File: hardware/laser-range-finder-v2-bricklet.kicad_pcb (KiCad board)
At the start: 2 copper layers, 48.2 x 35.6 mm, 23 parts, among them P1 CON-SENSOR2, P2 DEBUG, P3 BOOT, P4 CONN_6, U1 XMC1XXX24, U2 DRILL, U3 DRILL, U4 DRILL, U5 DRILL

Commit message: changed pcb design
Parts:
- added G***: Logo_31x31, kicad-libraries:Logo_31x31, F.Cu at (123.9, 100.1)
- added G***: LOGO, kicad-libraries:Logo_CoMCU, F.Cu at (146.2, 97.2)
- added VAL: CE_5mm, kicad-libraries:CE_5mm, F.Cu at (146.3, 103.4)
- added VAL: WEEE_7mm, kicad-libraries:WEEE_7mm, F.Cu at (145.2, 109.2)
- moved D1 31.0 mm to (156.8, 98.5), turned to 270 degrees
- moved D2 26.2 mm to (156.8, 109.2), turned to 270 degrees
- moved RP2 10.0 mm to (141.2, 99.8), turned to 270 degrees
- moved C6 4.48 mm to (122.1, 107.8), turned to 180 degrees
- moved C5 3.17 mm to (122.2, 111.9), turned to 0 degrees
- moved C7 2.39 mm to (126.2, 109.2), turned to 270 degrees
- moved L1 1.98 mm to (122.2, 109.9), turned to 0 degrees
- moved U5 1.53 mm to (141.9, 88.4)
- moved U2 1.49 mm to (126.9, 118.4)
- moved U3 1.38 mm to (141.9, 118.4)
- moved U4 1.35 mm to (126.9, 88.4)
- moved RP1 0.91 mm to (124.3, 104.3)
- moved P4 0.85 mm to (134.4, 113.5)
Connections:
- C4 pad 2: GND -> Net-(C4-Pad2)
- D1 pad 1: Net-(D1-Pad1) -> 3V3
- D1 pad 2: 3V3 -> Net-(D1-Pad2)
- D2 pad 1: Net-(D2-Pad1) -> 3V3
- D2 pad 2: 3V3 -> Net-(D2-Pad2)
- L1 pad 1: Net-(C6-Pad1) -> +5V
- L1 pad 2: +5V -> Net-(C6-Pad1)
- RP2 pad 1: Net-(D1-Pad1) -> Net-(D1-Pad2)
- RP2 pad 4: Net-(D2-Pad1) -> Net-(D2-Pad2)
- U1 pad 9: GND -> Net-(C4-Pad2)
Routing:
- net GND: track 56.9 -> 35.8 mm
- net Net-(D2-Pad2): track 0.00 -> 18.4 mm
- net Net-(D1-Pad2): track 0.00 -> 15.0 mm
- net Net-(D2-Pad1): track 9.66 -> 0.00 mm
- net Net-(D1-Pad1): track 7.82 -> 0.00 mm
- net Net-(C4-Pad2): track 0.00 -> 6.81 mm, vias 0 -> 3
- net Net-(C6-Pad1): track 16.8 -> 11.9 mm
- net Net-(RP2-Pad8): track 6.02 -> 10.7 mm
- net Net-(RP2-Pad5): track 5.94 -> 9.00 mm
- net 3V3: track 74.6 -> 77.1 mm
- net (no net): track 1.47 -> 0.00 mm
- net SDA: track 20.9 -> 21.6 mm
- net ENABLE: track 8.71 -> 8.05 mm
- net S-MOSI: track 7.66 -> 7.05 mm
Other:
- outline, holes or cut-outs redrawn
- net class Default: via_dia 0.5 -> 0.55; via_drill 0.15 -> 0.25
- board text added: "Distance"
- board text added: "Laser Range Finder 2.0"
- board text added: "Status"
- board text added: "tinkerforge.com"

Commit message: changed pcb design
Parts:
- P4: value CONN_6 -> JST_GHR_6
- RP2: value R_PACK4 -> 1k
- moved RP1 4.39 mm to (119.9, 104.9)
- moved G*** 1.68 mm to (124.4, 101.7)
- moved VAL 0.86 mm to (145.7, 110.0)
- moved G*** 0.30 mm to (146.2, 96.8)
- moved D1 0.30 mm to (156.8, 98.2)
- moved VAL 0.28 mm to (146.2, 103.7)
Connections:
- C4 pad 2: Net-(C4-Pad2) -> GND
- P4 pad EP: (no net) -> GND
- U1 pad 9: Net-(C4-Pad2) -> GND
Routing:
- net GND: track 35.8 -> 59.6 mm, vias 16 -> 23
- net Net-(C4-Pad2): track 6.81 -> 0.00 mm, vias 3 -> 0
- net S-CLK: track 6.93 -> 11.5 mm
- net S-CS: track 6.80 -> 11.4 mm
- net S-MOSI: track 7.05 -> 11.6 mm
- net Net-(P1-Pad6): track 6.96 -> 2.38 mm
- net Net-(P1-Pad5): track 6.78 -> 2.21 mm
- net S-MISO: track 8.42 -> 13.0 mm
- net Net-(P1-Pad4): track 6.59 -> 2.40 mm
- net Net-(C1-Pad1): track 7.06 -> 3.13 mm
- net 3V3: track 77.1 -> 78.6 mm

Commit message: some minor improvements
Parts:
- RP3: value 4k7 -> 1k
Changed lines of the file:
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@@
-(kicad_pcb (version 20171130) (host pcbnew 5.0.0-fee4fd1~66~ubuntu16.04.1)
+(kicad_pcb (version 20171130) (host pcbnew 5.0.0-fee4fd1~66~ubuntu18.04.1)
   (general
     (thickness 1.6002)
@@
   )
   (setup
-    (last_trace_width 0.3)
+    (last_trace_width 0.2)
     (user_trace_width 0.29972)
     (user_trace_width 0.3)
@@
     (aux_axis_origin 134.55 85.85)
     (grid_origin 130.875 104.4)
-    (visible_elements FFFFFF9F)
+    (visible_elements FFFFFFFF)
     (pcbplotparams
       (layerselection 0x00030_80000001)
@@
       (effects (font (size 0.29972 0.29972) (thickness 0.07493)))
     )
-    (fp_text value 4k7 (at 1.01 -0.02 180) (layer F.Fab)
+    (fp_text value 1k (at 1.01 -0.02 180) (layer F.Fab)
       (effects (font (size 0.29972 0.29972) (thickness 0.07493)))
     )

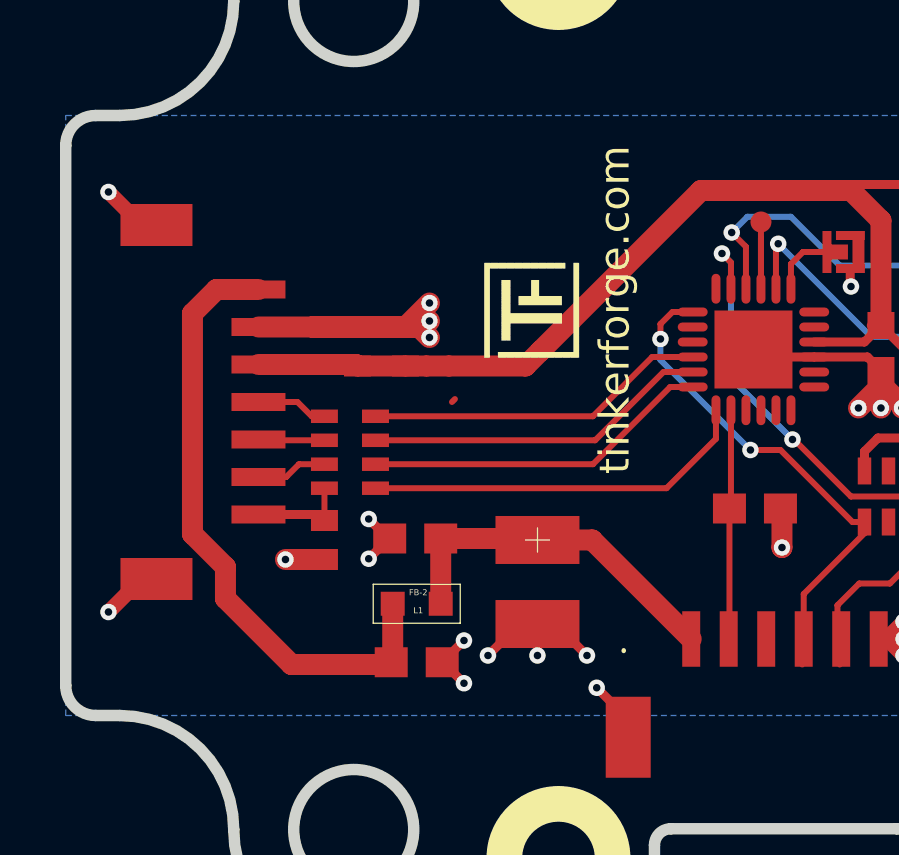
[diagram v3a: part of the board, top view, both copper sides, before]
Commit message: changed footprints C2, C3, RP1
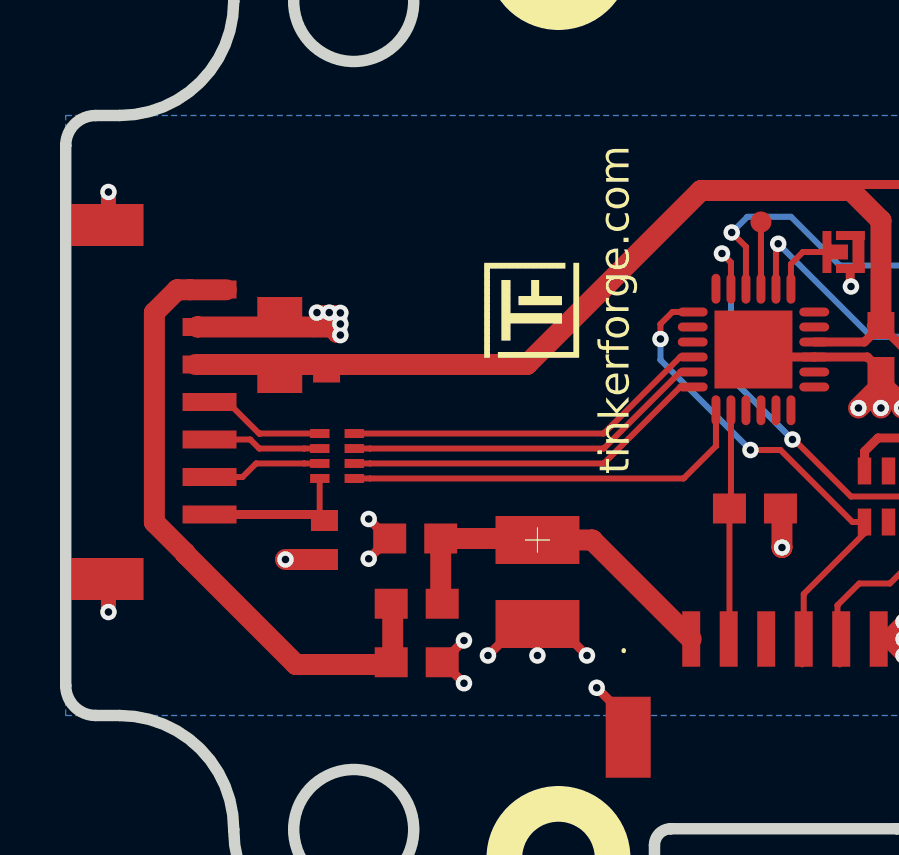
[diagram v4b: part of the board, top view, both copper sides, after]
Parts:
- C2: footprint C0402E -> C0805E
- C3: footprint C0402E -> C0603F
- L1: footprint 0603 -> R0603E
- RP1: footprint 4X0603 -> 4X0402
- moved C3 2.63 mm to (119.1, 101.3)
- moved C2 2.59 mm to (117.6, 101.3)
- moved P1 1.63 mm to (110.6, 103.2)
- moved RP1 0.45 mm to (119.5, 105.0), turned to 270 degrees
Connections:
- RP1 pad 1: Net-(C1-Pad1) -> Net-(P1-Pad4)
- RP1 pad 2: Net-(P1-Pad6) -> Net-(P1-Pad5)
- RP1 pad 3: Net-(P1-Pad5) -> Net-(P1-Pad6)
- RP1 pad 4: Net-(P1-Pad4) -> Net-(C1-Pad1)
- RP1 pad 5: S-CS -> S-MISO
- RP1 pad 6: S-CLK -> S-MOSI
- RP1 pad 7: S-MOSI -> S-CLK
- RP1 pad 8: S-MISO -> S-CS
- RP3 pad 5: 3V3 -> Net-(RP3-Pad5)
- RP3 pad 8: 3V3 -> Net-(RP3-Pad5)
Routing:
- net GND: track 59.6 -> 46.4 mm, vias 23 -> 25
- net 3V3: track 78.6 -> 75.6 mm
- net Net-(P1-Pad4): track 2.40 -> 4.34 mm
- net Net-(C1-Pad1): track 3.13 -> 4.90 mm
- net Net-(P1-Pad5): track 2.21 -> 3.80 mm
- net Net-(P1-Pad6): track 2.38 -> 3.86 mm
- net S-CS: track 11.4 -> 12.3 mm
- net S-CLK: track 11.5 -> 12.3 mm
- net S-MISO: track 13.0 -> 13.7 mm
- net S-MOSI: track 11.6 -> 12.3 mm
- net +5V: track 21.0 -> 21.6 mm
